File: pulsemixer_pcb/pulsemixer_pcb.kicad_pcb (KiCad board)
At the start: 2 copper layers, 68 parts, among them SW101 SW_PG_RIGHT, SW102 SW_PG_LEFT, SW103 SW_STRM_DEV, SW201 Vol_Encoder, SW202 SW_MUTE, SW301 Vol_Encoder, SW302 SW_MUTE, SW401 Vol_Encoder, SW402 SW_MUTE, SW501 Vol_Encoder, SW502 SW_MUTE, U201 MCP23017_SP, U301 MCP23017_SP, U501 MCP23017_SP

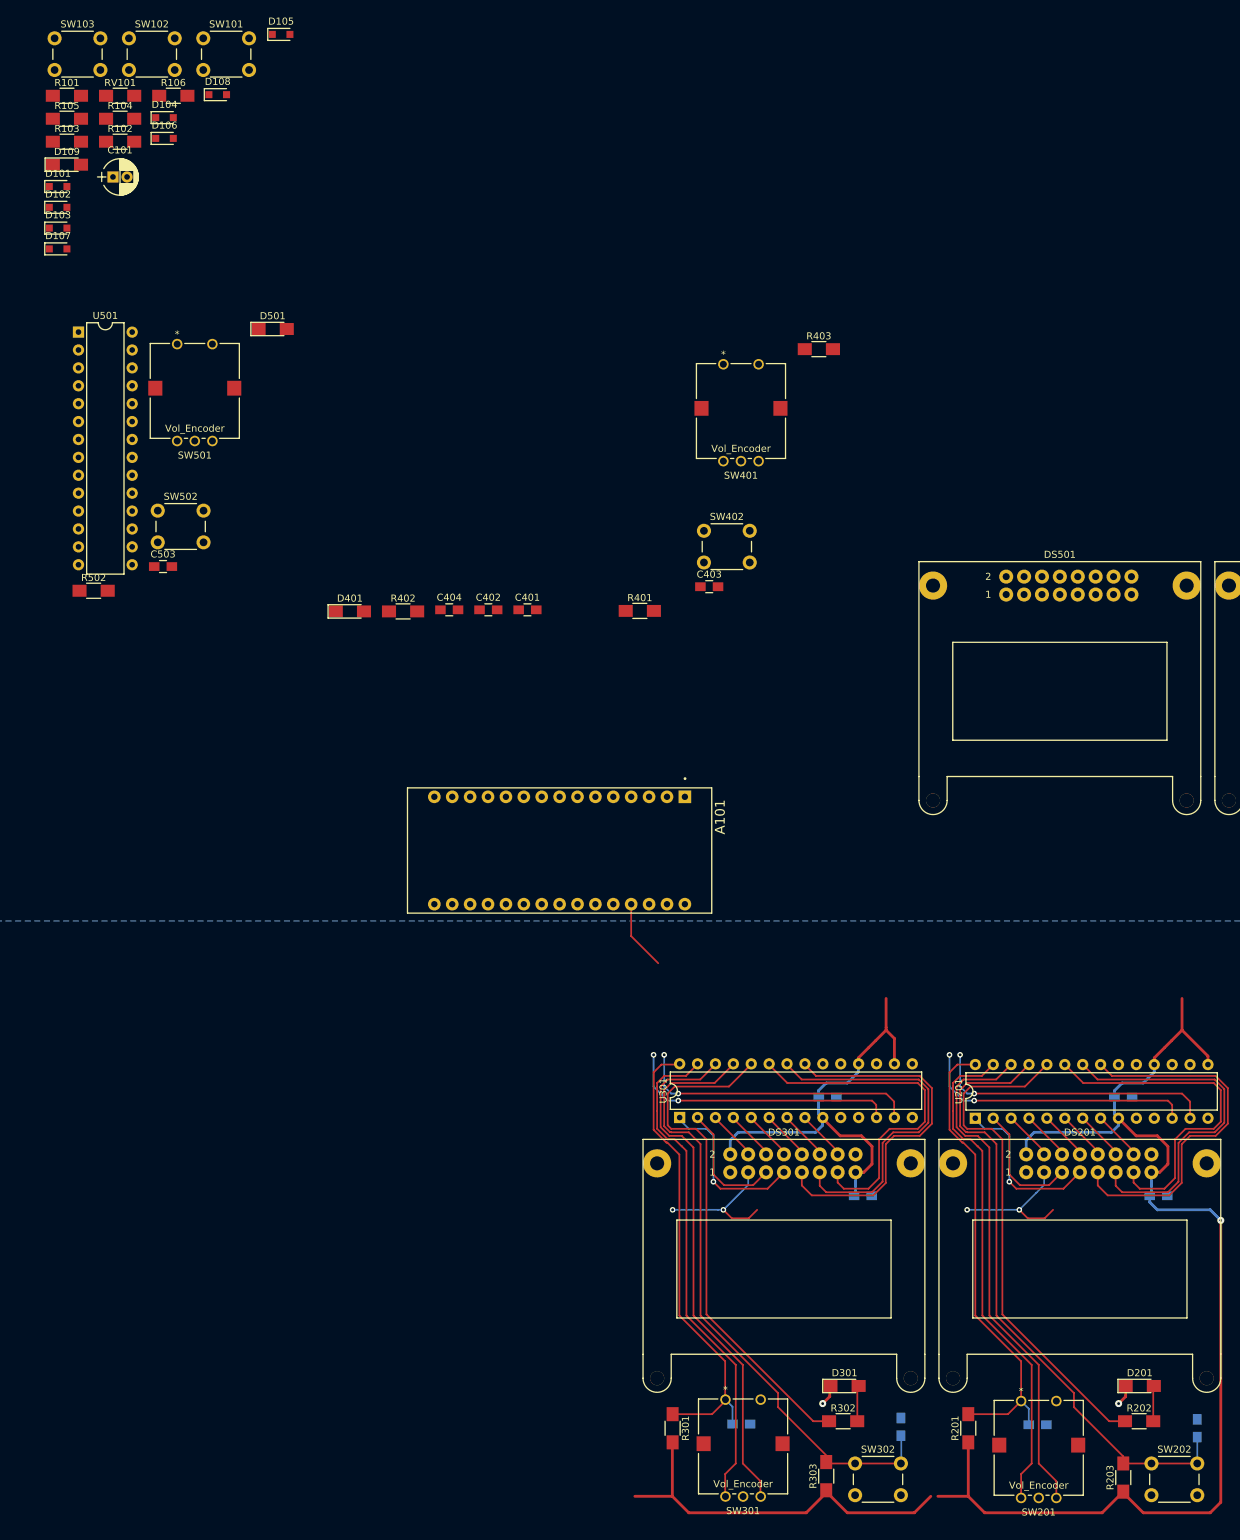
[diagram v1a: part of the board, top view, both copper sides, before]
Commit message: Simple reading of rotary encoder through the GPIO expander, with interrupts.
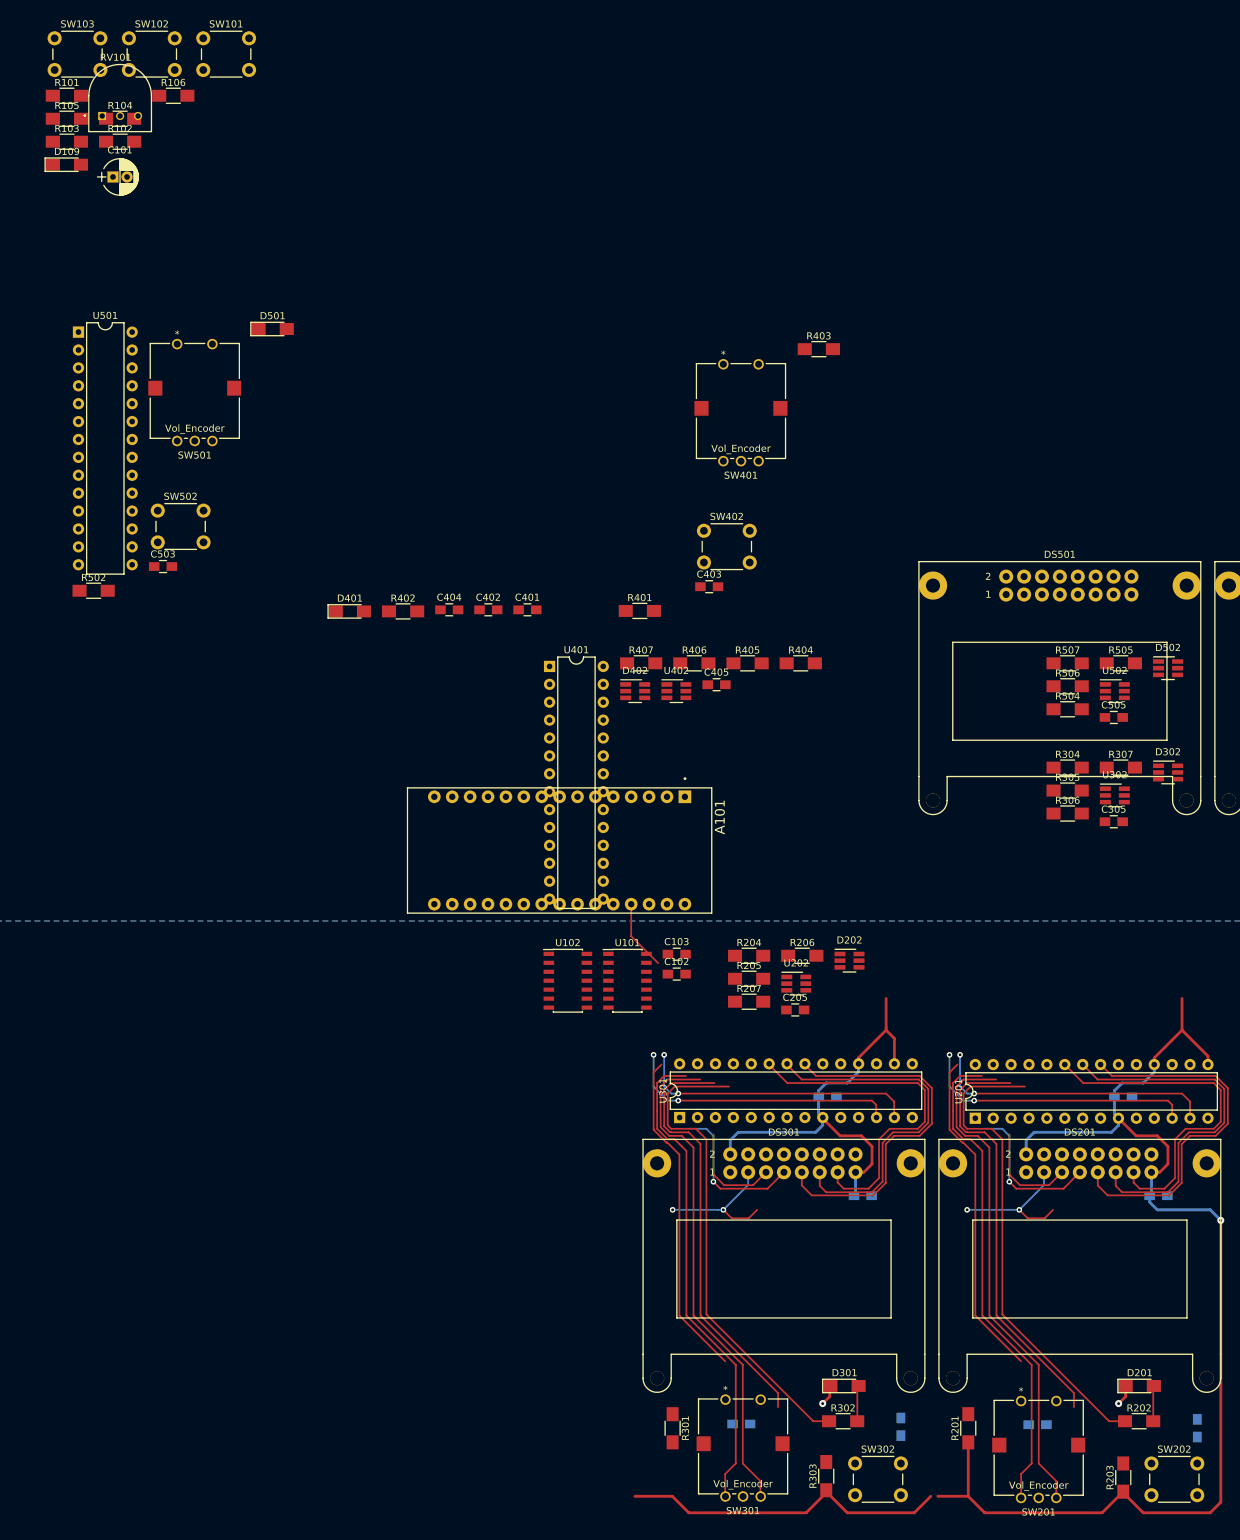
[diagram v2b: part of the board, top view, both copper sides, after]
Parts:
- removed D101, D102, D103, D104, D105, D106, D107, D108: DIODE, Diodes_SMD:D_SOD-323_HandSoldering
- added C102: 0.1µ, Capacitors_SMD:C_0805_HandSoldering, F.Cu at (112.8, 29.5)
- added C103: 0.1µ, Capacitors_SMD:C_0805_HandSoldering, F.Cu at (112.8, 26.7)
- added C205: 0.1µ, Capacitors_SMD:C_0805_HandSoldering, F.Cu at (129.6, 34.6)
- added C305: 0.1µ, Capacitors_SMD:C_0805_HandSoldering, F.Cu at (174.8, 7.92)
- added C405: 0.1µ, Capacitors_SMD:C_0805_HandSoldering, F.Cu at (118.4, -11.5)
- added C505: 0.1µ, Capacitors_SMD:C_0805_HandSoldering, F.Cu at (174.8, -6.88)
- added D202: BAT54DW-7-F, TO_SOT_Packages_SMD:SOT-23-6_Handsoldering, F.Cu at (137.3, 27.6)
- added D302: BAT54DW-7-F, TO_SOT_Packages_SMD:SOT-23-6_Handsoldering, F.Cu at (182.5, 0.93)
- added D402: BAT54DW-7-F, TO_SOT_Packages_SMD:SOT-23-6_Handsoldering, F.Cu at (106.9, -10.6)
- added D502: BAT54DW-7-F, TO_SOT_Packages_SMD:SOT-23-6_Handsoldering, F.Cu at (182.5, -13.9)
- added R204: 10K, Resistors_SMD:R_1206_HandSoldering, F.Cu at (123.1, 26.9)
- added R205: 10K, Resistors_SMD:R_1206_HandSoldering, F.Cu at (123.1, 30.2)
- added R206: 1K, Resistors_SMD:R_1206_HandSoldering, F.Cu at (130.6, 26.9)
- added R207: 1K, Resistors_SMD:R_1206_HandSoldering, F.Cu at (123.1, 33.5)
- added R304: 10K, Resistors_SMD:R_1206_HandSoldering, F.Cu at (168.3, 0.24)
- added R305: 10K, Resistors_SMD:R_1206_HandSoldering, F.Cu at (168.3, 3.50)
- added R306: 1K, Resistors_SMD:R_1206_HandSoldering, F.Cu at (168.3, 6.76)
- added R307: 1K, Resistors_SMD:R_1206_HandSoldering, F.Cu at (175.8, 0.24)
- added R404: 10K, Resistors_SMD:R_1206_HandSoldering, F.Cu at (130.4, -14.6)
- added R405: 10K, Resistors_SMD:R_1206_HandSoldering, F.Cu at (122.8, -14.6)
- added R406: 1K, Resistors_SMD:R_1206_HandSoldering, F.Cu at (115.3, -14.6)
- added R407: 1K, Resistors_SMD:R_1206_HandSoldering, F.Cu at (107.7, -14.6)
- added R504: 10K, Resistors_SMD:R_1206_HandSoldering, F.Cu at (168.3, -8.04)
- added R505: 10K, Resistors_SMD:R_1206_HandSoldering, F.Cu at (175.8, -14.6)
- added R506: 1K, Resistors_SMD:R_1206_HandSoldering, F.Cu at (168.3, -11.3)
- added R507: 1K, Resistors_SMD:R_1206_HandSoldering, F.Cu at (168.3, -14.6)
- added U101: SN74LHC08DR, Housings_SOIC:SOIC-14_3.9x8.7mm_Pitch1.27mm, F.Cu at (105.8, 30.5)
- added U102: SN74HC21DR, Housings_SOIC:SOIC-14_3.9x8.7mm_Pitch1.27mm, F.Cu at (97.3, 30.5)
- added U202: 74LVC2G14, TO_SOT_Packages_SMD:SOT-23-6_Handsoldering, F.Cu at (129.8, 30.9)
- added U302: 74LVC2G14, TO_SOT_Packages_SMD:SOT-23-6_Handsoldering, F.Cu at (175.0, 4.19)
- added U401: MCP23017_SP, Housings_DIP:DIP-28_W7.62mm, F.Cu at (94.7, -14.1)
- added U402: 74LVC2G14, TO_SOT_Packages_SMD:SOT-23-6_Handsoldering, F.Cu at (112.7, -10.6)
- added U502: 74LVC2G14, TO_SOT_Packages_SMD:SOT-23-6_Handsoldering, F.Cu at (175.0, -10.6)
- RV101: footprint Resistors_SMD:R_1206_HandSoldering -> pulsemixer_pcb:TRIM_3352T-1-103LF
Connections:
- A101 pad 10: /PAGE_RIGHT_BTN -> /INTCH0
- A101 pad 11: (no net) -> /STRM_DEV_LED
- A101 pad 12: (no net) -> /STRM_DEV
- A101 pad 13: (no net) -> /PAGE_LEFT_BTN
- A101 pad 14: (no net) -> /PAGE_RIGHT_BTN
- A101 pad 5: (no net) -> /INTBTN
- A101 pad 6: (no net) -> /INTVOL
- A101 pad 7: /STRM_DEV_LED -> /INTCH3
- A101 pad 8: /STRM_DEV -> /INTCH2
- A101 pad 9: /PAGE_LEFT_BTN -> /INTCH1
- C201 pad 2: /Channel1/MUTE_SW -> Net-(C201-Pad2)
- C202 pad 2: /Channel1/VOL_SW -> Net-(C202-Pad2)
- C301 pad 2: /Channel2/MUTE_SW -> Net-(C301-Pad2)
- C302 pad 2: /Channel2/VOL_SW -> Net-(C302-Pad2)
- C401 pad 2: /Channel3/MUTE_SW -> Net-(C401-Pad2)
- C402 pad 2: /Channel3/VOL_SW -> Net-(C402-Pad2)
- C501 pad 2: /Channel0/MUTE_SW -> Net-(C501-Pad2)
- C502 pad 2: /Channel0/VOL_SW -> Net-(C502-Pad2)
- R201 pad 2: /Channel1/VOL_SW -> Net-(D202-Pad4)
- R203 pad 2: /Channel1/MUTE_SW -> Net-(D202-Pad1)
- R301 pad 2: /Channel2/VOL_SW -> Net-(D302-Pad4)
- R303 pad 2: /Channel2/MUTE_SW -> Net-(D302-Pad1)
- R401 pad 2: /Channel3/VOL_SW -> Net-(D402-Pad4)
- R403 pad 2: /Channel3/MUTE_SW -> Net-(D402-Pad1)
- R501 pad 2: /Channel0/VOL_SW -> Net-(D502-Pad4)
- R503 pad 2: /Channel0/MUTE_SW -> Net-(D502-Pad1)
- SW201 pad S1: /Channel1/VOL_SW -> Net-(D202-Pad4)
- SW202 pad 1: /Channel1/MUTE_SW -> Net-(D202-Pad1)
- SW301 pad S1: /Channel2/VOL_SW -> Net-(D302-Pad4)
- SW302 pad 1: /Channel2/MUTE_SW -> Net-(D302-Pad1)
- SW401 pad S1: /Channel3/VOL_SW -> Net-(D402-Pad4)
- SW402 pad 1: /Channel3/MUTE_SW -> Net-(D402-Pad1)
- SW501 pad S1: /Channel0/VOL_SW -> Net-(D502-Pad4)
- SW502 pad 1: /Channel0/MUTE_SW -> Net-(D502-Pad1)
- U201 pad 1: /Channel1/LCD_DB0 -> /Channel1/MUTE_SW
- U201 pad 19: (no net) -> /INTBTN_CH1
- U201 pad 2: /Channel1/LCD_RW -> /Channel1/VOL_SW
- U201 pad 20: (no net) -> /INTVOL_CH1
- U201 pad 24: /Channel1/MUTE_LED -> /Channel1/LCD_DB5
- U201 pad 25: /Channel1/MUTE_SW -> /Channel1/LCD_DB7
- U201 pad 26: /Channel1/VOL_B -> /Channel1/MUTE_LED
- U201 pad 27: /Channel1/VOL_A -> /Channel1/VOL_B
- U201 pad 28: /Channel1/VOL_SW -> /Channel1/VOL_A
- U201 pad 3: /Channel1/LCD_RS -> /Channel1/LCD_DB0
- U201 pad 4: /Channel1/LCD_E -> /Channel1/LCD_RW
- U201 pad 5: /Channel1/LCD_DB1 -> /Channel1/LCD_RS
- U201 pad 6: /Channel1/LCD_DB3 -> /Channel1/LCD_E
- U201 pad 7: /Channel1/LCD_DB5 -> /Channel1/LCD_DB1
- U201 pad 8: /Channel1/LCD_DB7 -> /Channel1/LCD_DB3
- U301 pad 1: /Channel2/LCD_DB0 -> /Channel2/MUTE_SW
- U301 pad 11: Net-(U301-Pad11) -> (no net)
- U301 pad 14: Net-(U301-Pad14) -> (no net)
- U301 pad 19: /Channel2/INTB -> /INTBTN_CH2
- U301 pad 2: /Channel2/LCD_RW -> /Channel2/VOL_SW
- U301 pad 20: /Channel2/INTA -> /INTVOL_CH2
- U301 pad 24: /Channel2/MUTE_LED -> /Channel2/LCD_DB5
- U301 pad 25: /Channel2/MUTE_SW -> /Channel2/LCD_DB7
- U301 pad 26: /Channel2/VOL_B -> /Channel2/MUTE_LED
- U301 pad 27: /Channel2/VOL_A -> /Channel2/VOL_B
- U301 pad 28: /Channel2/VOL_SW -> /Channel2/VOL_A
- U301 pad 3: /Channel2/LCD_RS -> /Channel2/LCD_DB0
- U301 pad 4: /Channel2/LCD_E -> /Channel2/LCD_RW
- U301 pad 5: /Channel2/LCD_DB1 -> /Channel2/LCD_RS
- U301 pad 6: /Channel2/LCD_DB3 -> /Channel2/LCD_E
- U301 pad 7: /Channel2/LCD_DB5 -> /Channel2/LCD_DB1
- U301 pad 8: /Channel2/LCD_DB7 -> /Channel2/LCD_DB3
- U501 pad 1: /Channel0/LCD_DB0 -> /Channel0/MUTE_SW
- U501 pad 19: (no net) -> /INTBTN_CH0
- U501 pad 2: /Channel0/LCD_RW -> /Channel0/VOL_SW
- U501 pad 20: (no net) -> /INTVOL_CH0
- U501 pad 24: /Channel0/MUTE_LED -> /Channel0/LCD_DB5
- U501 pad 25: /Channel0/MUTE_SW -> /Channel0/LCD_DB7
- U501 pad 26: /Channel0/VOL_B -> /Channel0/MUTE_LED
- U501 pad 27: /Channel0/VOL_A -> /Channel0/VOL_B
- U501 pad 28: /Channel0/VOL_SW -> /Channel0/VOL_A
- U501 pad 3: /Channel0/LCD_RS -> /Channel0/LCD_DB0
- U501 pad 4: /Channel0/LCD_E -> /Channel0/LCD_RW
- U501 pad 5: /Channel0/LCD_DB1 -> /Channel0/LCD_RS
- U501 pad 6: /Channel0/LCD_DB3 -> /Channel0/LCD_E
- U501 pad 7: /Channel0/LCD_DB5 -> /Channel0/LCD_DB1
- U501 pad 8: /Channel0/LCD_DB7 -> /Channel0/LCD_DB3
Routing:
- net /Channel2/MUTE_SW: track 89.7 -> 60.8 mm
- net /Channel1/MUTE_SW: track 89.7 -> 60.8 mm
- net /sheet5F077D1F/VOL_SW: track 67.2 -> 46.9 mm
- net /Channel1/VOL_SW: track 67.1 -> 46.9 mm
- net +5V: track 295.8 -> 288.2 mm
- net /Channel2/LCD_RS: track 7.07 -> 0.45 mm
- net /Channel2/LCD_DB7: track 7.07 -> 0.45 mm
- net /Channel2/LCD_DB5: track 7.07 -> 0.45 mm
- net /Channel2/LCD_DB1: track 7.07 -> 0.45 mm
- net /Channel1/LCD_E: track 7.07 -> 0.45 mm
- net /Channel1/LCD_DB7: track 7.07 -> 0.45 mm
- net /Channel1/LCD_DB5: track 7.07 -> 0.45 mm
- net /Channel1/LCD_DB1: track 7.07 -> 0.45 mm
- net /Channel2/LCD_E: track 7.07 -> 0.45 mm
- net /Channel2/LCD_DB3: track 7.07 -> 0.45 mm
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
